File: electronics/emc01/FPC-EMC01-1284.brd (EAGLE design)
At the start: 100 x 86.6 mm, 73 parts, among them J1 CONN-RECT-26PIN-2ROWSHROUDED, J10 ICSP, J11 CONN-RECT-16PIN-2ROW, J12 CONN-RECT-16PIN-2ROW, J13 CONN-RECT-16PIN-2ROW, J14 CONN-RECT-16PIN-2ROW, J15 CONN-RECT-16PIN-2ROW, J2 PCIE, J4 MOT-X, J5 MOT-Y, J6 MOT-Z, J7 CONN-RECT-3PINJST_PH_2MM, J8 CONN-RECT-3PINJST_PH_2MM, J9 CONN-RECT-3PINJST_PH_2MM, Q4 16Mhz, U10 MCP4728, U2 A4982, U3 A4982, U4 A4982, U5 ATMEGA1284P-AU

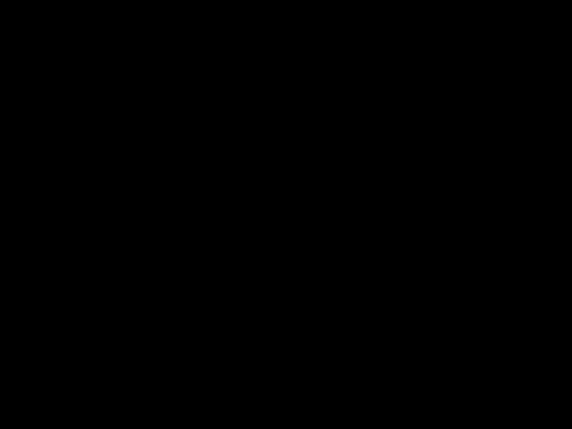
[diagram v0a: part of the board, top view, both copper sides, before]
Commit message: Changed connector on LCD board.  Added notes to EMC01 board.
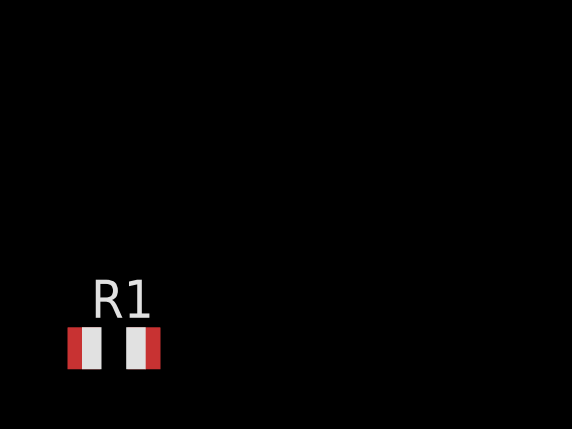
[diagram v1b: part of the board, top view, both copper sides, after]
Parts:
- added R1: 10k, adafruit:R0805
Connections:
- new net N$1: J2.6, R1.2
- new net N$3: R1.1, U5.44
- net GND: no longer J2.6
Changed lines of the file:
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@@
 </element>
 <element name="S1" library="SparkFun" package="TACTILE_SWITCH_SMD" value="" x="23.26" y="67.456" rot="R330"/>
+<element name="R1" library="adafruit" package="R0805" value="10k" x="1.8" y="3.6"/>
 </elements>
 <signals>
@@
 <contactref element="C39" pad="2"/>
 <contactref element="J2" pad="5"/>
-<contactref element="J2" pad="6"/>
 <contactref element="J2" pad="4"/>
 <contactref element="C6" pad="-"/>
@@
 <contactref element="S1" pad="2"/>
 <contactref element="S1" pad="1"/>
-<wire x1="67.172" y1="80.01" x2="71.006" y2="84.836" width="0" layer="19" extent="1-1"/>
+<wire x1="81.239965625" y1="77.413146875" x2="79.969965625" y2="79.61285" width="0" layer="19" extent="1-1"/>
+<wire x1="72.441146875" y1="72.333146875" x2="81.239965625" y2="77.413146875" width="0" layer="19" extent="1-1"/>
+<wire x1="68.0417375" y1="69.793146875" x2="72.441146875" y2="72.333146875" width="0" layer="19" extent="1-1"/>
+<wire x1="66.7717375" y1="71.99285" x2="68.0417375" y2="69.793146875" width="0" layer="19" extent="1-1"/>
+<wire x1="67.172" y1="80.01" x2="66.7717375" y2="71.99285" width="0" layer="19" extent="1-1"/>
+<wire x1="71.006" y1="84.836" x2="67.172" y2="80.01" width="0" layer="19" extent="1-1"/>
 <wire x1="60.284" y1="77.232" x2="67.172" y2="80.01" width="0" layer="19" extent="1-1"/>
 <wire x1="56.9745125" y1="76.31405625" x2="60.284" y2="77.232" width="0" layer="19" extent="1-1"/>
@@
 <wire x1="28.006" y1="82.804" x2="29.022" y2="80.264" width="0" layer="19" extent="1-1"/>
 <wire x1="27.439146875" y1="75.80285" x2="29.022" y2="80.264" width="0" layer="19" extent="1-1"/>
+<wire x1="23.0397375" y1="78.34285" x2="27.439146875" y2="75.80285" width="0" layer="19" extent="1-1"/>
+<wire x1="21.7697375" y1="76.143146875" x2="23.0397375" y2="78.34285" width="0" layer="19" extent="1-1"/>
 <wire x1="22.01279375" y1="70.375778125" x2="21.7697375" y2="76.143146875" width="0" layer="19" extent="1-1"/>
 <wire x1="17.781325" y1="69.125" x2="22.01279375" y2="70.375778125" width="0" layer="19" extent="1-1"/>
 <wire x1="26.412203125" y1="67.835778125" x2="22.01279375" y2="70.375778125" width="0" layer="19" extent="1-1"/>
+<wire x1="36.237965625" y1="70.72285" x2="38.166" y2="77.216" width="0" layer="19" extent="1-1"/>
+<wire x1="34.967965625" y1="68.523146875" x2="36.237965625" y2="70.72285" width="0" layer="19" extent="1-1"/>
 <wire x1="39.86805" y1="64.22236875" x2="34.967965625" y2="68.523146875" width="0" layer="19" extent="1-1"/>
-<wire x1="64.886" y1="32.512" x2="58.89" y2="29.27" width="0" layer="19" extent="1-1"/>
-<wire x1="28.264" y1="60.9135375" x2="26.037965625" y2="54.45885" width="0" layer="19" extent="1-1"/>
-<wire x1="68.894346875" y1="39.033196875" x2="64.886" y2="32.512" width="0" layer="19" extent="1-1"/>
-<wire x1="73.5153875" y1="39.887075" x2="68.894346875" y2="39.033196875" width="0" layer="19" extent="1-1"/>
-<wire x1="73.014" y1="43.434" x2="73.5153875" y2="39.887075" width="0" layer="19" extent="1-1"/>
-<wire x1="76.846" y1="37.338" x2="73.5153875" y2="39.887075" width="0" layer="19" extent="1-1"/>
-<wire x1="74.052" y1="34.544" x2="76.846" y2="37.338" width="0" layer="19" extent="1-1"/>
-<wire x1="67.32330625" y1="43.462075" x2="68.894346875" y2="39.033196875" width="0" layer="19" extent="1-1"/>
-<wire x1="64.5" y1="43.434" x2="67.32330625" y2="43.462075" width="0" layer="19" extent="1-1"/>
-<wire x1="62.468" y1="40.132" x2="64.5" y2="43.434" width="0" layer="19" extent="1-1"/>
-<wire x1="57.592" y1="38.354" x2="62.468" y2="40.132" width="0" layer="19" extent="1-1"/>
-<wire x1="68.564" y1="49.784" x2="67.32330625" y2="43.462075" width="0" layer="19" extent="1-1"/>
+<wire x1="48.514" y1="62.23" x2="46.45" y2="68.871" width="0" layer="19" extent="1-1"/>
+<wire x1="28.264" y1="60.9135375" x2="26.412203125" y2="67.835778125" width="0" layer="19" extent="1-1"/>
+<wire x1="26.037965625" y1="54.45885" x2="28.264" y2="60.9135375" width="0" layer="19" extent="1-1"/>
+<wire x1="24.767965625" y1="52.259146875" x2="26.037965625" y2="54.45885" width="0" layer="19" extent="1-1"/>
 <wire x1="20.966" y1="45.466" x2="24.767965625" y2="52.259146875" width="0" layer="19" extent="1-1"/>
 <wire x1="23.738" y1="44.45" x2="20.966" y2="45.466" width="0" layer="19" extent="1-1"/>
@@
 <wire x1="36.052" y1="45.72" x2="35.676690625" y2="38.265921875" width="0" layer="19" extent="1-1"/>
 <wire x1="36.56" y1="49.784" x2="36.052" y2="45.72" width="0" layer="19" extent="1-1"/>
+<wire x1="60.795" y1="65.697259375" x2="53.6" y2="68.871" width="0" layer="19" extent="1-1"/>
+<wire x1="62.065" y1="63.49755625" x2="60.795" y2="65.697259375" width="0" layer="19" extent="1-1"/>
 <wire x1="61.51" y1="85.77" x2="67.172" y2="80.01" width="0" layer="19" extent="1-1"/>
-<wire x1="78.3767625" y1="27.6073875" x2="74.052" y2="34.544" width="0" layer="19" extent="1-1"/>
 <wire x1="45.940921875" y1="54.059075" x2="48.514" y2="62.23" width="0" layer="19" extent="1-1"/>
 <wire x1="54.059075" y1="54.059075" x2="45.940921875" y2="54.059075" width="0" layer="19" extent="1-1"/>
@@
 <wire x1="45.4" y1="39.624" x2="45.940921875" y2="45.940921875" width="0" layer="19" extent="1-1"/>
 <wire x1="16.419234375" y1="36.621609375" x2="24.014" y2="40.64" width="0" layer="19" extent="1-1"/>
+<wire x1="12.8397375" y1="62.07885" x2="17.781325" y2="69.125" width="0" layer="19" extent="1-1"/>
+<wire x1="11.5697375" y1="59.879146875" x2="12.8397375" y2="62.07885" width="0" layer="19" extent="1-1"/>
+<wire x1="17.239146875" y1="59.53885" x2="12.8397375" y2="62.07885" width="0" layer="19" extent="1-1"/>
+<wire x1="15.969146875" y1="57.339146875" x2="17.239146875" y2="59.53885" width="0" layer="19" extent="1-1"/>
+<wire x1="57.592" y1="38.354" x2="54.61585" y2="46.4977" width="0" layer="19" extent="1-1"/>
+<wire x1="62.468" y1="40.132" x2="57.592" y2="38.354" width="0" layer="19" extent="1-1"/>
+<wire x1="64.5" y1="43.434" x2="62.468" y2="40.132" width="0" layer="19" extent="1-1"/>
+<wire x1="67.32330625" y1="43.462075" x2="64.5" y2="43.434" width="0" layer="19" extent="1-1"/>
+<wire x1="68.894346875" y1="39.033196875" x2="67.32330625" y2="43.462075" width="0" layer="19" extent="1-1"/>
+<wire x1="73.5153875" y1="39.887075" x2="68.894346875" y2="39.033196875" width="0" layer="19" extent="1-1"/>
+<wire x1="73.014" y1="43.434" x2="73.5153875" y2="39.887075" width="0" layer="19" extent="1-1"/>
+<wire x1="76.846" y1="37.338" x2="73.5153875" y2="39.887075" width="0" layer="19" extent="1-1"/>
+<wire x1="74.052" y1="34.544" x2="76.846" y2="37.338" width="0" layer="19" extent="1-1"/>
+<wire x1="68.564" y1="49.784" x2="67.32330625" y2="43.462075" width="0" layer="19" extent="1-1"/>
+<wire x1="64.886" y1="32.512" x2="68.894346875" y2="39.033196875" width="0" layer="19" extent="1-1"/>
+<wire x1="58.89" y1="29.27" x2="64.886" y2="32.512" width="0" layer="19" extent="1-1"/>
+<wire x1="78.3767625" y1="27.6073875" x2="74.052" y2="34.544" width="0" layer="19" extent="1-1"/>
+<wire x1="54.2" y1="90.75" x2="61.51" y2="85.77" width="0" layer="19" extent="1-1"/>
+<wire x1="50" y1="90.75" x2="54.2" y2="90.75" width="0" layer="19" extent="1-1"/>
+<wire x1="43.65" y1="26.73" x2="38.338" y2="34.29" width="0" layer="19" extent="1-1"/>
+<wire x1="77.4317375" y1="53.529146875" x2="68.564" y2="49.784" width="0" layer="19" extent="1-1"/>
+<wire x1="76.1617375" y1="55.72885" x2="77.4317375" y2="53.529146875" width="0" layer="19" extent="1-1"/>
 <wire x1="86.5" y1="48.768" x2="77.4317375" y2="53.529146875" width="0" layer="19" extent="1-1"/>
+<wire x1="39.84" y1="15.969" x2="43.65" y2="26.73" width="0" layer="19" extent="1-1"/>
+<wire x1="44.92" y1="13.429" x2="39.84" y2="15.969" width="0" layer="19" extent="1-1"/>
+<wire x1="50" y1="15.969" x2="44.92" y2="13.429" width="0" layer="19" extent="1-1"/>
+<wire x1="57.62" y1="15.969" x2="50" y2="15.969" width="0" layer="19" extent="1-1"/>
+<wire x1="65.24" y1="13.429" x2="57.62" y2="15.969" width="0" layer="19" extent="1-1"/>
+<wire x1="90.629965625" y1="61.149146875" x2="86.5" y2="48.768" width="0" layer="19" extent="1-1"/>
+<wire x1="89.359965625" y1="63.34885" x2="90.629965625" y2="61.149146875" width="0" layer="19" extent="1-1"/>
 <wire x1="92.71" y1="15.24" x2="78.3767625" y2="27.6073875" width="0" layer="19" extent="1-1"/>
 </signal>
@@
 <contactref element="J3" pad="1"/>
 </signal>
+<signal name="N$1">
+<contactref element="J2" pad="6"/>
+<contactref element="R1" pad="2"/>
+<wire x1="2.8" y1="3.6" x2="45.8" y2="90.75" width="0" layer="19" extent="1-1"/>
+</signal>
+<signal name="N$3">
+<contactref element="U5" pad="44"/>
+<contactref element="R1" pad="1"/>
+<wire x1="0.8" y1="3.6" x2="43.121121875" y2="51.239275" width="0" layer="19" extent="1-1"/>
+</signal>
 </signals>

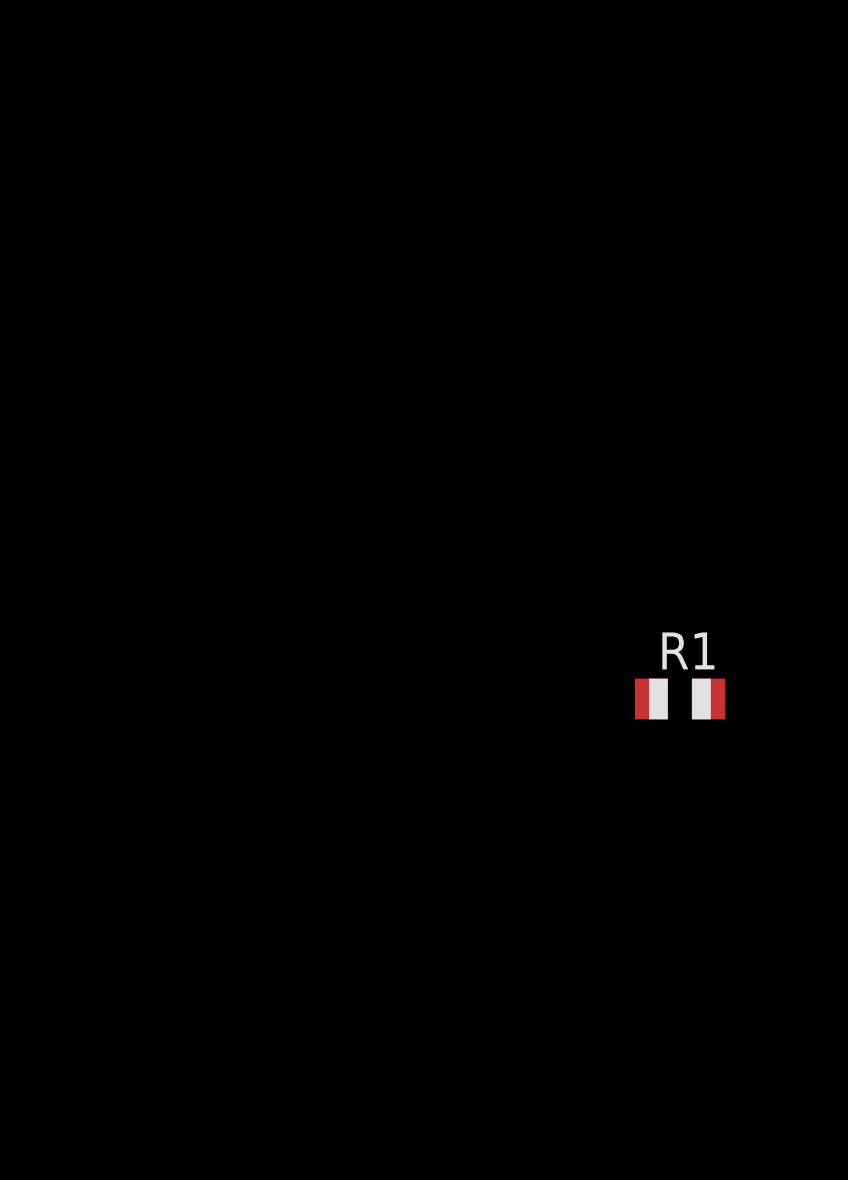
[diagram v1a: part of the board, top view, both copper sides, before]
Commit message: Forgot how to Eagle, but added DC/DC. Change components for better specs
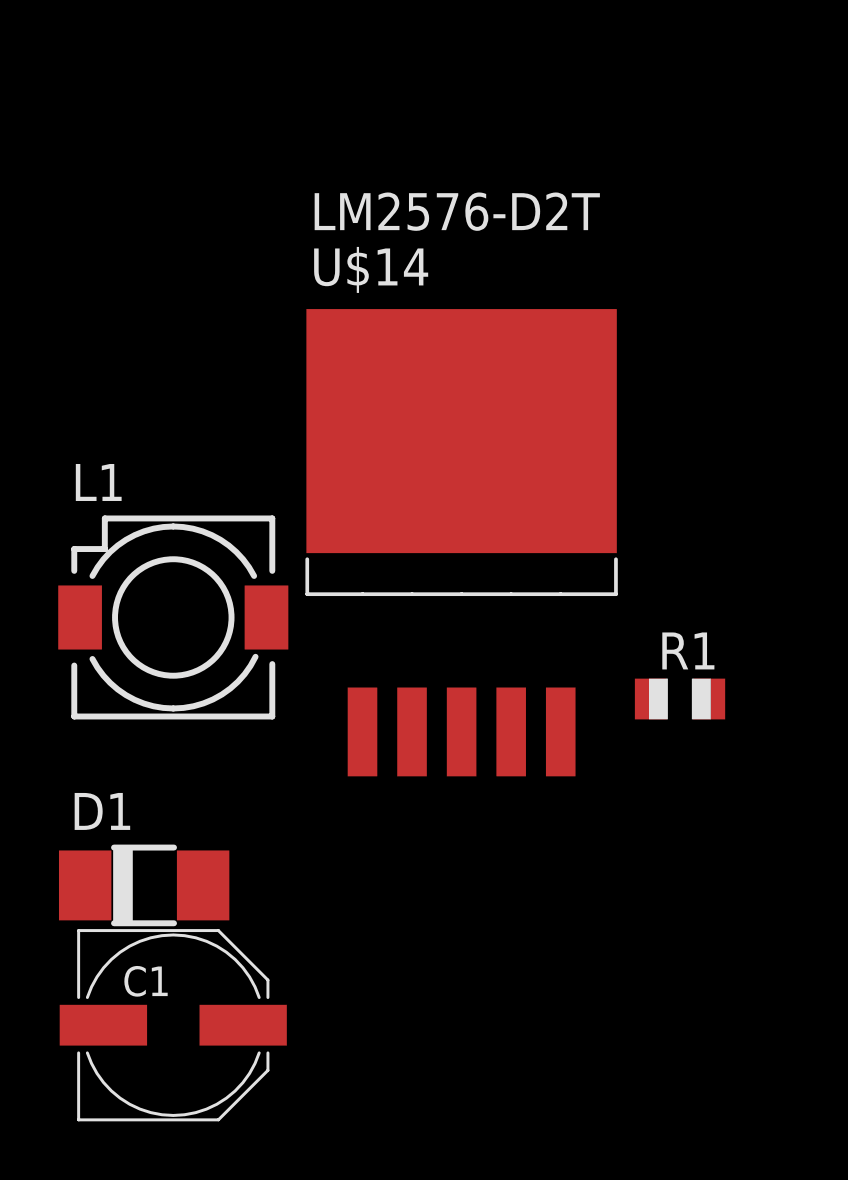
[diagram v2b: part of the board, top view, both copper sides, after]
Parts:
- added C1: 470uF, rcl:PANASONIC_D
- added D1: (no value), diode:DO-214AC
- added L1: SLF7045, inductors:SLF7045
- added U$14: LM2576-D2T, FirePick:D2PAK
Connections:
- new net N$4: D1.C, L1.1, U$14.2
- new net N$5: C1.+, L1.2, U$14.4
- net 12V: now also U$14.1
- net GND: now also C1.-, D1.A, U$14.3, U$14.5, U$14.6
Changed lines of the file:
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@@
 <layer number="97" name="Info" color="7" fill="1" visible="no" active="no"/>
 <layer number="98" name="Guide" color="6" fill="1" visible="no" active="no"/>
+<layer number="99" name="SpiceOrder" color="5" fill="1" visible="no" active="no"/>
 <layer number="100" name="Muster" color="7" fill="1" visible="no" active="no"/>
 <layer number="101" name="Patch_Top" color="12" fill="4" visible="no" active="yes"/>
@@
 <element name="S1" library="SparkFun" package="TACTILE_SWITCH_SMD" value="" x="23.26" y="67.456" rot="R330"/>
 <element name="R1" library="adafruit" package="R0805" value="10k" x="1.8" y="3.6"/>
+<element name="U$14" library="FirePick" package="D2PAK" value="LM2576-D2T" x="-5.7" y="12.8"/>
+<element name="L1" library="inductors" package="SLF7045" value="SLF7045" x="-15.6" y="6.4"/>
+<element name="D1" library="diode" package="DO-214AC" value="" x="-16.6" y="-2.8"/>
+<element name="C1" library="rcl" package="PANASONIC_D" value="470uF" x="-15.6" y="-7.6"/>
 </elements>
 <signals>
@@
 <contactref element="S1" pad="2"/>
 <contactref element="S1" pad="1"/>
+<contactref element="U$14" pad="3"/>
+<contactref element="U$14" pad="6"/>
+<contactref element="U$14" pad="5"/>
+<contactref element="D1" pad="A"/>
+<contactref element="C1" pad="-"/>
 <wire x1="81.239965625" y1="77.413146875" x2="79.969965625" y2="79.61285" width="0" layer="19" extent="1-1"/>
 <wire x1="72.441146875" y1="72.333146875" x2="81.239965625" y2="77.413146875" width="0" layer="19" extent="1-1"/>
@@
 <wire x1="89.359965625" y1="63.34885" x2="90.629965625" y2="61.149146875" width="0" layer="19" extent="1-1"/>
 <wire x1="92.71" y1="15.24" x2="78.3767625" y2="27.6073875" width="0" layer="19" extent="1-1"/>
+<wire x1="-5.7" y1="12.8" x2="16.419234375" y2="36.621609375" width="0" layer="19" extent="1-1"/>
+<wire x1="-5.7" y1="2.47" x2="-5.7" y2="12.8" width="0" layer="19" extent="1-1"/>
+<wire x1="-2.296" y1="2.47" x2="-5.7" y2="2.47" width="0" layer="19" extent="1-1"/>
+<wire x1="-14.575" y1="-2.8" x2="-5.7" y2="2.47" width="0" layer="19" extent="1-1"/>
+<wire x1="-18" y1="-7.6" x2="-14.575" y2="-2.8" width="0" layer="19" extent="1-1"/>
 </signal>
 <signal name="12V">
@@
 <contactref element="J14" pad="2"/>
 <contactref element="C9" pad="+"/>
+<contactref element="U$14" pad="1"/>
 <wire x1="64.57203125" y1="70.72285" x2="75.806" y2="84.836" width="0" layer="19" extent="1-1"/>
 <wire x1="65.84203125" y1="68.523146875" x2="64.57203125" y2="70.72285" width="0" layer="19" extent="1-1"/>
@@
 <wire x1="32.882" y1="32.512" x2="31.17335625" y2="35.665921875" width="0" layer="19" extent="1-1"/>
 <wire x1="32.88" y1="27.686" x2="32.882" y2="32.512" width="0" layer="19" extent="1-1"/>
+<wire x1="-9.104" y1="2.47" x2="32.88" y2="27.686" width="0" layer="19" extent="1-1"/>
 </signal>
 <signal name="MISO">
@@
 <wire x1="0.8" y1="3.6" x2="43.121121875" y2="51.239275" width="0" layer="19" extent="1-1"/>
 </signal>
+<signal name="N$4">
+<contactref element="L1" pad="1"/>
+<contactref element="U$14" pad="2"/>
+<contactref element="D1" pad="C"/>
+<wire x1="-18.8" y1="6.4" x2="-18.625" y2="-2.8" width="0" layer="19" extent="1-1"/>
+<wire x1="-7.402" y1="2.47" x2="-18.8" y2="6.4" width="0" layer="19" extent="1-1"/>
+</signal>
+<signal name="N$5">
+<contactref element="U$14" pad="4"/>
+<contactref element="L1" pad="2"/>
+<contactref element="C1" pad="+"/>
+<wire x1="-3.998" y1="2.47" x2="-13.2" y2="-7.6" width="0" layer="19" extent="1-1"/>
+<wire x1="-12.4" y1="6.4" x2="-3.998" y2="2.47" width="0" layer="19" extent="1-1"/>
+</signal>
 </signals>
